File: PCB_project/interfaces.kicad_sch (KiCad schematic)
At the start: 21 parts, among them J14 Molex 104031-0811, J4 USB_C_Receptacle_USB2.0, U11 USBLC6-2SC6-ES, U13 W25Q256

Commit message: Schematic updated
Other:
- title: KP-PTR -> KP-PTR project - PTR_mini
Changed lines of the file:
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@@
 	(paper "A4")
 	(title_block
-		(title "KP-PTR")
-		(date "2023-12-10")
-		(rev "1.1")
+		(title "KP-PTR project - PTR_mini")
+		(date "2026-09-17")
+		(rev "1.0")
 		(company "Polskie Towarzystwo Rakietowe")
 		(comment 1 "bartekM, FlyingBanana, Kretu, Red Labs, Stachu M, U.S. air force i inni")

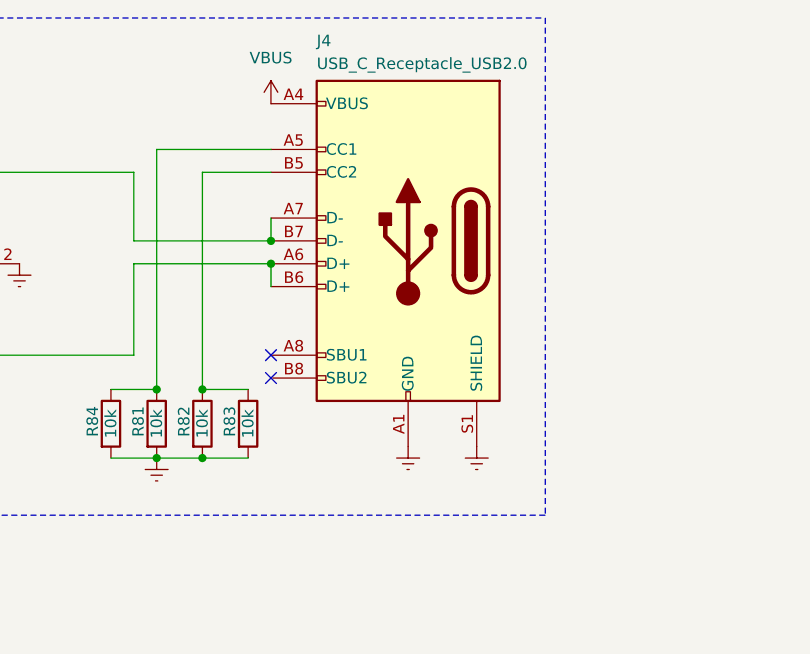
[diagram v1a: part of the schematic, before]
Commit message: + USB connector changed to SMD
+ igniters connectors changed to single 6 pin connector
+ buzzer selected
+ crystal changed to TCXO (experimental)
+ JLC production files generated
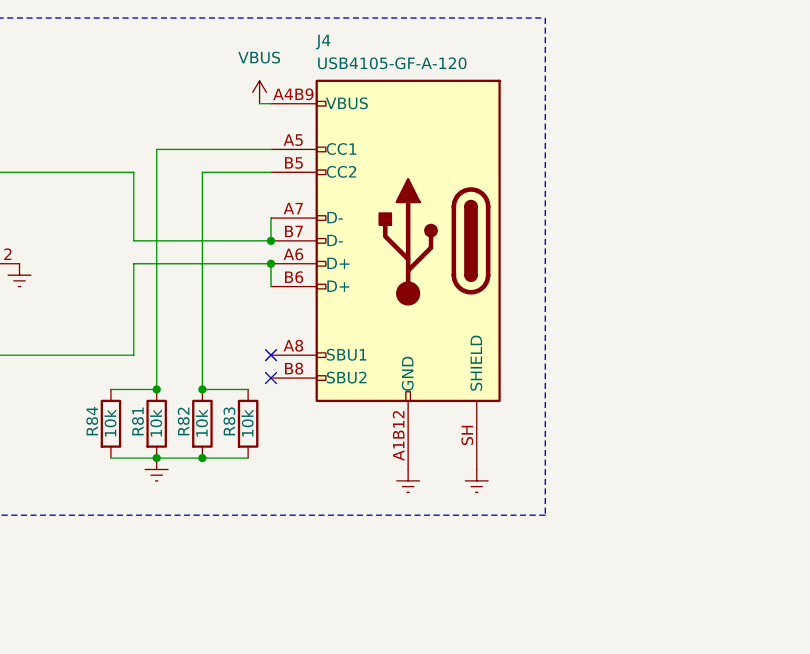
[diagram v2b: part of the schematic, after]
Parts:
- C66: footprint Capacitor_SMD:C_0402_1005Metric -> Capacitor_SMD:C_0603_1608Metric
- J4: value USB_C_Receptacle_USB2.0 -> USB4105-GF-A-120; footprint KP-PTR_lib:USB_C_213716 -> KP-PTR_lib:USB_C_16P_SMD_USB4105-GF-A
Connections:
- net Earth: now also J4.A1B12 (GND), J4.B1A12 (GND), J4.SH (SHIELD); no longer J4.A1 (GND), J4.A12 (GND), J4.B1 (GND), J4.B12 (GND), J4.S1 (SHIELD)
- net VBUS: now also J4.A4B9 (VBUS), J4.B4A9 (VBUS); no longer J4.A4 (VBUS), J4.A9 (VBUS), J4.B4 (VBUS), J4.B9 (VBUS)
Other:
- moved on the sheet: J4
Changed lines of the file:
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@@
 		)
 	)
+	(wire
+		(pts
+			(xy 90.17 26.67) (xy 91.44 26.67)
+		)
+		(stroke
+			(width 0)
+			(type default)
+		)
+	)
 	(polyline
 		(pts
@@
 	(symbol
 		(lib_id "power:VBUS")
-		(at 91.44 26.67 0)
+		(at 90.17 26.67 0)
 		(unit 1)
 		(body_style 1)
@@
 		(fields_autoplaced yes)
 		(property "Reference" "#PWR0126"
-			(at 91.44 30.48 0)
+			(at 90.17 30.48 0)
 			(hide yes)
 			(show_name no)
@@
 		)
 		(property "Value" "VBUS"
-			(at 91.44 21.59 0)
+			(at 90.17 21.59 0)
 			(show_name no)
 			(do_not_autoplace no)
@@
 		)
 		(property "Footprint" ""
-			(at 91.44 26.67 0)
+			(at 90.17 26.67 0)
 			(hide yes)
 			(show_name no)
@@
 		)
 		(property "Datasheet" ""
-			(at 91.44 26.67 0)
+			(at 90.17 26.67 0)
 			(hide yes)
 			(show_name no)
@@
 		)
 		(property "Description" ""
-			(at 91.44 26.67 0)
+			(at 90.17 26.67 0)
 			(show_name no)
 			(do_not_autoplace no)
@@
 	(symbol
 		(lib_id "power:Earth")
-		(at 114.3 64.77 0)
+		(at 114.3 67.31 0)
 		(unit 1)
 		(body_style 1)
@@
 		(fields_autoplaced yes)
 		(property "Reference" "#PWR0138"
-			(at 114.3 71.12 0)
+			(at 114.3 73.66 0)
 			(hide yes)
 			(show_name no)
@@
 		)
 		(property "Value" "Earth"
-			(at 114.3 68.58 0)
+			(at 114.3 71.12 0)
 			(hide yes)
 			(show_name no)
@@
 		)
 		(property "Footprint" ""
-			(at 114.3 64.77 0)
+			(at 114.3 67.31 0)
 			(hide yes)
 			(show_name no)
@@
 		)
 		(property "Datasheet" ""
-			(at 114.3 64.77 0)
+			(at 114.3 67.31 0)
 			(hide yes)
 			(show_name no)
@@
 		)
 		(property "Description" ""
-			(at 114.3 64.77 0)
+			(at 114.3 67.31 0)
 			(show_name no)
 			(do_not_autoplace no)
@@
 	(symbol
 		(lib_id "power:Earth")
-		(at 106.68 64.77 0)
+		(at 106.68 67.31 0)
 		(unit 1)
 		(body_style 1)
@@
 		(fields_autoplaced yes)
 		(property "Reference" "#PWR0137"
-			(at 106.68 71.12 0)
+			(at 106.68 73.66 0)
 			(hide yes)
 			(show_name no)
@@
 		)
 		(property "Value" "Earth"
-			(at 106.68 68.58 0)
+			(at 106.68 71.12 0)
 			(hide yes)
 			(show_name no)
@@
 		)
 		(property "Footprint" ""
-			(at 106.68 64.77 0)
+			(at 106.68 67.31 0)
 			(hide yes)
 			(show_name no)
@@
 		)
 		(property "Datasheet" ""
-			(at 106.68 64.77 0)
+			(at 106.68 67.31 0)
 			(hide yes)
 			(show_name no)
@@
 		)
 		(property "Description" ""
-			(at 106.68 64.77 0)
+			(at 106.68 67.31 0)
 			(show_name no)
 			(do_not_autoplace no)
@@
 			)
 		)
-		(property "Footprint" "Capacitor_SMD:C_0402_1005Metric"
+		(property "Footprint" "Capacitor_SMD:C_0603_1608Metric"
 			(at 169.8752 162.56 0)
 			(hide yes)
@@
 			)
 		)
-		(property "Value" "USB_C_Receptacle_USB2.0"
+		(property "Value" "USB4105-GF-A-120"
 			(at 96.52 22.225 0)
 			(show_name no)
@@
 			)
 		)
-		(property "Footprint" "KP-PTR_lib:USB_C_213716"
+		(property "Footprint" "KP-PTR_lib:USB_C_16P_SMD_USB4105-GF-A"
 			(at 102.87 41.91 0)
 			(hide yes)
@@
 			)
 		)
-		(pin "A1"
+		(pin "B1A12"
 		)
-		(pin "A12"
+		(pin "SH"
 		)
-		(pin "A4"
+		(pin "A1B12"
 		)
 		(pin "A5"
@@
 		(pin "A8"
 		)
-		(pin "A9"
+		(pin "A4B9"
 		)
-		(pin "B1"
-		)
-		(pin "B12"
-		)
-		(pin "B4"
+		(pin "B4A9"
 		)
 		(pin "B5"
@@
 		(pin "B8"
 		)
-		(pin "B9"
-		)
-		(pin "S1"
-		)
 		(instances
